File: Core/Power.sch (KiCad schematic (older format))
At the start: 16 parts, among them J6 Conn_02x08_Odd_Even, U4 TL072, U5 MIC5504-3.3YM5, U8 TL072

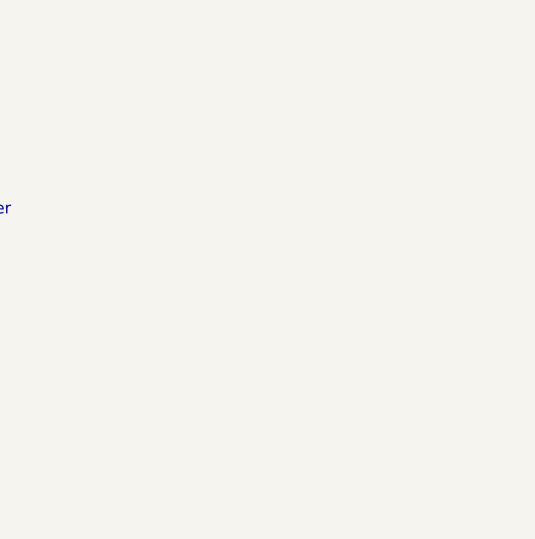
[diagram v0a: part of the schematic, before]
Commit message: Add external EEPROM and RAM
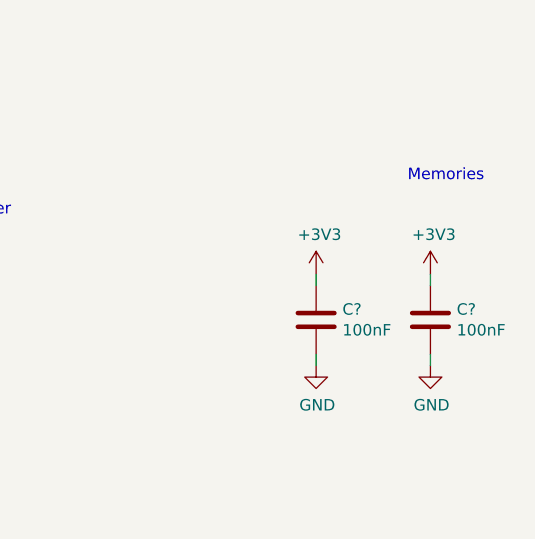
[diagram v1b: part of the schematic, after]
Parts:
- added C? (x2): 100nF, Capacitor_SMD:C_0603_1608Metric, symbol Device:C
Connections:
- net +3V3: now also C?.1, C?.1
- net GND: now also C?.2, C?.2
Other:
- note added: "Memories"
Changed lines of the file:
@@
 Wire Wire Line
 	7250 2000 6600 2000
+Wire Wire Line
+	8700 4950 8700 5000
+Wire Wire Line
+	8700 5350 8700 5300
+$Comp
+L Device:C C?
+U 1 1 62D056ED
+P 8700 5150
+F 0 "C?" H 8815 5196 50  0000 L CNN
+F 1 "100nF" H 8815 5105 50  0000 L CNN
+F 2 "Capacitor_SMD:C_0603_1608Metric" H 8738 5000 50  0001 C CNN
+F 3 "~" H 8700 5150 50  0001 C CNN
+	1    8700 5150
+	1    0    0    -1
+$EndComp
+$Comp
+L Device:C C?
+U 1 1 62D056F7
+P 9200 5150
+F 0 "C?" H 9315 5196 50  0000 L CNN
+F 1 "100nF" H 9315 5105 50  0000 L CNN
+F 2 "Capacitor_SMD:C_0603_1608Metric" H 9238 5000 50  0001 C CNN
+F 3 "~" H 9200 5150 50  0001 C CNN
+	1    9200 5150
+	1    0    0    -1
+$EndComp
+$Comp
+L power:+3V3 #PWR?
+U 1 1 62D05701
+P 8700 4950
+F 0 "#PWR?" H 8700 4800 50  0001 C CNN
+F 1 "+3V3" H 8715 5123 50  0000 C CNN
+F 2 "" H 8700 4950 50  0001 C CNN
+F 3 "" H 8700 4950 50  0001 C CNN
+	1    8700 4950
+	1    0    0    -1
+$EndComp
+$Comp
+L power:+3V3 #PWR?
+U 1 1 62D0570B
+P 9200 4950
+F 0 "#PWR?" H 9200 4800 50  0001 C CNN
+F 1 "+3V3" H 9215 5123 50  0000 C CNN
+F 2 "" H 9200 4950 50  0001 C CNN
+F 3 "" H 9200 4950 50  0001 C CNN
+	1    9200 4950
+	1    0    0    -1
+$EndComp
+$Comp
+L power:GND #PWR?
+U 1 1 62D05715
+P 8700 5350
+F 0 "#PWR?" H 8700 5100 50  0001 C CNN
+F 1 "GND" H 8705 5177 50  0000 C CNN
+F 2 "" H 8700 5350 50  0001 C CNN
+F 3 "" H 8700 5350 50  0001 C CNN
+	1    8700 5350
+	1    0    0    -1
+$EndComp
+$Comp
+L power:GND #PWR?
+U 1 1 62D0571F
+P 9200 5350
+F 0 "#PWR?" H 9200 5100 50  0001 C CNN
+F 1 "GND" H 9205 5177 50  0000 C CNN
+F 2 "" H 9200 5350 50  0001 C CNN
+F 3 "" H 9200 5350 50  0001 C CNN
+	1    9200 5350
+	1    0    0    -1
+$EndComp
+Wire Wire Line
+	9200 5350 9200 5300
+Wire Wire Line
+	9200 5000 9200 4950
+Text Notes 9100 4550 0    50   ~ 0
+Memories
 $EndSCHEMATC

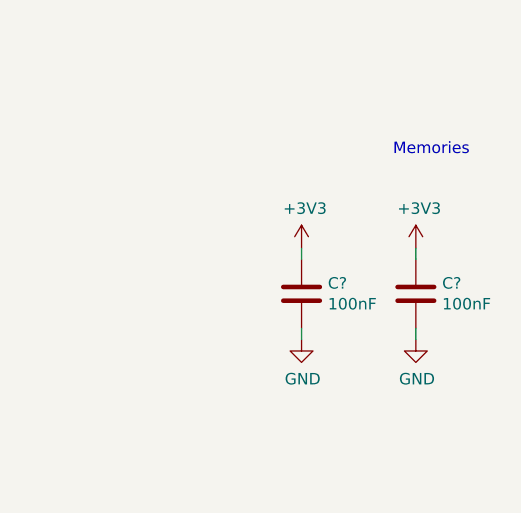
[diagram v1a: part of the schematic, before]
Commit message: Add IO and bootloader buttons
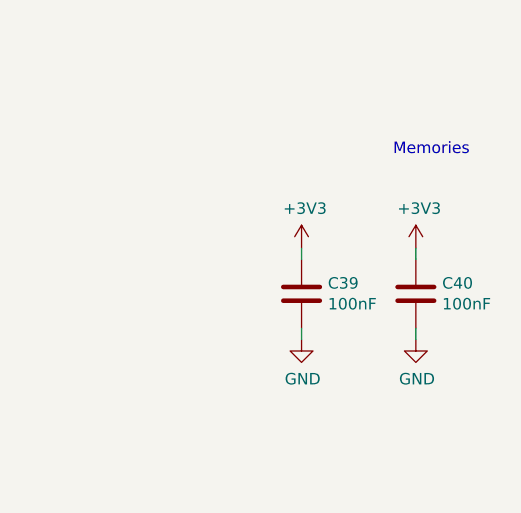
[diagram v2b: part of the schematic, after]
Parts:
- gave numbers to parts that had none: 2
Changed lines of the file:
@@
 	8700 5350 8700 5300
 $Comp
-L Device:C C?
+L Device:C C39
 U 1 1 62D056ED
 P 8700 5150
-F 0 "C?" H 8815 5196 50  0000 L CNN
+F 0 "C39" H 8815 5196 50  0000 L CNN
 F 1 "100nF" H 8815 5105 50  0000 L CNN
 F 2 "Capacitor_SMD:C_0603_1608Metric" H 8738 5000 50  0001 C CNN
@@
 $EndComp
 $Comp
-L Device:C C?
+L Device:C C40
 U 1 1 62D056F7
 P 9200 5150
-F 0 "C?" H 9315 5196 50  0000 L CNN
+F 0 "C40" H 9315 5196 50  0000 L CNN
 F 1 "100nF" H 9315 5105 50  0000 L CNN
 F 2 "Capacitor_SMD:C_0603_1608Metric" H 9238 5000 50  0001 C CNN
@@
 $EndComp
 $Comp
-L power:+3V3 #PWR?
+L power:+3V3 #PWR0198
 U 1 1 62D05701
 P 8700 4950
-F 0 "#PWR?" H 8700 4800 50  0001 C CNN
+F 0 "#PWR0198" H 8700 4800 50  0001 C CNN
 F 1 "+3V3" H 8715 5123 50  0000 C CNN
 F 2 "" H 8700 4950 50  0001 C CNN
@@
 $EndComp
 $Comp
-L power:+3V3 #PWR?
+L power:+3V3 #PWR0199
 U 1 1 62D0570B
 P 9200 4950
-F 0 "#PWR?" H 9200 4800 50  0001 C CNN
+F 0 "#PWR0199" H 9200 4800 50  0001 C CNN
 F 1 "+3V3" H 9215 5123 50  0000 C CNN
 F 2 "" H 9200 4950 50  0001 C CNN
@@
 $EndComp
 $Comp
-L power:GND #PWR?
+L power:GND #PWR0200
 U 1 1 62D05715
 P 8700 5350
-F 0 "#PWR?" H 8700 5100 50  0001 C CNN
+F 0 "#PWR0200" H 8700 5100 50  0001 C CNN
 F 1 "GND" H 8705 5177 50  0000 C CNN
 F 2 "" H 8700 5350 50  0001 C CNN
@@
 $EndComp
 $Comp
-L power:GND #PWR?
+L power:GND #PWR0201
 U 1 1 62D0571F
 P 9200 5350
-F 0 "#PWR?" H 9200 5100 50  0001 C CNN
+F 0 "#PWR0201" H 9200 5100 50  0001 C CNN
 F 1 "GND" H 9205 5177 50  0000 C CNN
 F 2 "" H 9200 5350 50  0001 C CNN
